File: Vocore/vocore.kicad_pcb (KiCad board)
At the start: 4 copper layers, 58 x 58 mm, 126 parts, among them IC1 IC_ATMEGA32U4_TQFP44, J1 IO_USB-MICRO-B-MK5P, P2 IO_HOLE-3.2, P3 IO_HOLE-3.2, P3 PINHOLE, U1 IC_MP1484EN_SOIC08, U10 DLW21SN900SQ2, U11 C_SW_SPSDSMD, U13 IP4220CZ6, U14 IP4220CZ6, U15 AP2146, U16 AP2146, U17 C_SW_SPSDSMD, U2 DLW21SN900SQ2, U3 IP4220CZ6, U4 UPD720114-QFP48, U5 USB-AF-90, U8 FT232RL_SSOP_28, U9 DLW21SN900SQ2, X1 30MHz, X2 16m

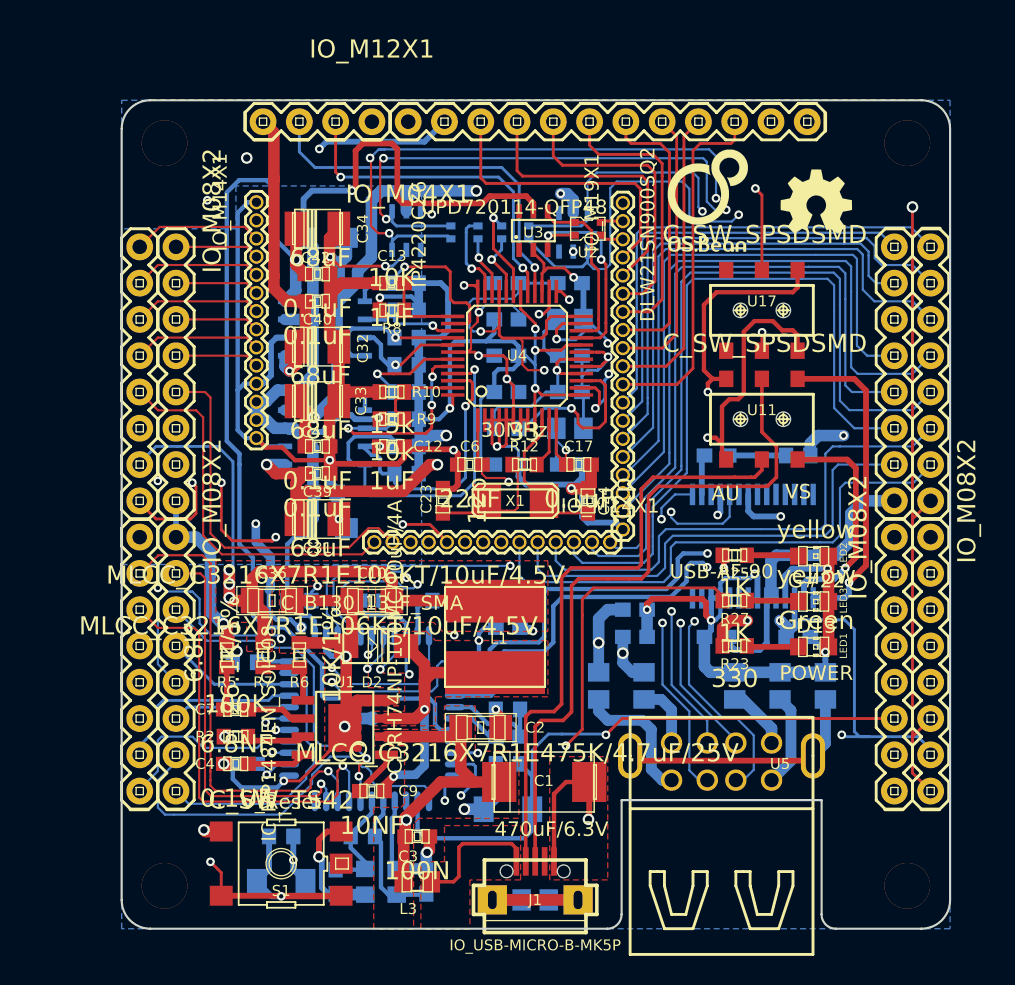
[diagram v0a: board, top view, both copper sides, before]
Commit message: Vocore第二版修改完成
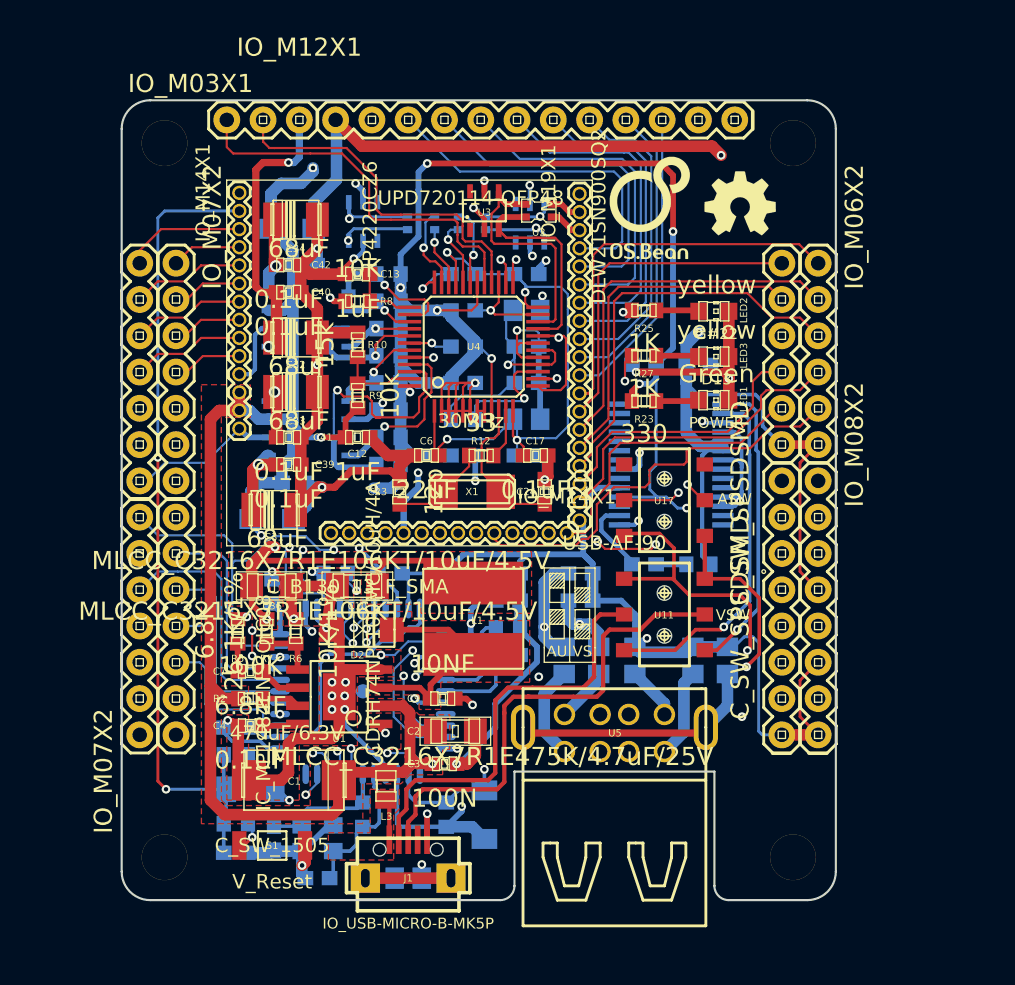
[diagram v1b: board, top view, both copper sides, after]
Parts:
- added C48: 104, C_C_0603, B.Cu at (87.0, 130.7)
- added R28: 200, C_R_0603, B.Cu at (87.0, 128.7)
- JP4: value IO_M08X2 -> IO_M06X2; footprint IO_M08X2 -> IO_M06X2
- JP5, JP6: value IO_M08X2 -> IO_M07X2; footprint IO_M08X2 -> IO_M07X2
- JP9: value IO_M04X1 -> IO_M03X1; footprint IO_M04X1 -> IO_M03X1
- S1: value C_SW_TS42 -> C_SW_1505; footprint C_SW_TS42 -> C_SW_1505
- moved JP6 55.3 mm to (82.8, 122.4)
- moved JP4 48.9 mm to (125.2, 89.4)
- moved C46 21.9 mm to (115.6, 96.5), turned to 0 degrees
- moved C47 19.1 mm to (119.4, 96.5), turned to 180 degrees
- moved LED1 18.6 mm to (120.7, 98.9)
- moved LED2 18.5 mm to (120.7, 92.7)
- moved LED3 18.5 mm to (120.7, 95.9)
- moved R25 18.3 mm to (115.6, 92.7)
- moved R23 18.3 mm to (115.6, 99.1)
- moved R27 18.3 mm to (115.6, 95.9)
- moved C1 17.5 mm to (91.1, 125.6), turned to 180 degrees
- moved U11 15.3 mm to (117.0, 114.0), turned to 90 degrees
- moved U17 14.9 mm to (117.0, 106.0), turned to 90 degrees
- moved R26 10.3 mm to (119.4, 110.5)
- moved JP9 10.2 mm to (86.4, 79.4), turned to 180 degrees
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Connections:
- JP2 pad 2: /G#26/LED4 -> (no net)
- JP2 pad 3: /G#25/LED3 -> (no net)
- JP2 pad 4: /G#24/LED2 -> (no net)
- JP2 pad 6: /G#23/LED1 -> (no net)
- JP3 pad 1: +3.3V -> (no net)
- JP4 pad 1: +5V -> /G#03/SPI_CS0
- JP4 pad 10: /ATMEGA32U4/D7 -> /G#13/PCM_DRX
- JP4 pad 11: /ATMEGA32U4/IO8 -> +5V
- JP4 pad 12: /ATMEGA32U4/IO9* -> +5V
- JP4 pad 2: GND -> /G#11/PCM_FS
- JP4 pad 3: /ATMEGA32U4/D0/RX -> /G#10/I2S_SDI/RXD
- JP4 pad 4: /ATMEGA32U4/D1/TX -> /G#06/SPI_MISO
- JP4 pad 5: /ATMEGA32U4/D2/SDA -> /G#08/I2S_WS/TDX
- JP4 pad 6: /ATMEGA32U4/D3/SCL -> /G#16/RXD2
- JP4 pad 7: /ATMEGA32U4/D4 -> /G#07/I2S_CLK
- JP4 pad 8: /ATMEGA32U4/D5* -> /G#15/TXD2
- JP4 pad 9: /ATMEGA32U4/D6* -> /G#14/PCM_DTX
- JP5 pad 10: /G#09/I2S_SD0 -> /G#05/SPI_MOSI
- JP5 pad 11: /G#05/SPI_MOSI -> /G#04/SPI_CLK
- JP5 pad 12: /G#04/SPI_CLK -> /G#09/I2S_SD0
- JP5 pad 13: +3.3V -> GND
- JP5 pad 14: /G#27/SPI_CS1 -> /G#12/PCM_CLK
- JP5 pad 9: /G#12/PCM_CLK -> /G#27/SPI_CS1
- JP6 pad 1: GND -> /ATMEGA32U4/D0/RX
- JP6 pad 10: /G#07/I2S_CLK -> /ATMEGA32U4/IO9*
- JP6 pad 11: /G#16/RXD2 -> /ATMEGA32U4/IO10*
- JP6 pad 12: /G#08/I2S_WS/TDX -> /ATMEGA32U4/IO11*
- JP6 pad 13: /G#06/SPI_MISO -> /ATMEGA32U4/IO12
- JP6 pad 14: /G#10/I2S_SDI/RXD -> /ATMEGA32U4/IO13*
- JP6 pad 2: +5V -> /ATMEGA32U4/D1/TX
- JP6 pad 3: /G#23/LED1 -> /ATMEGA32U4/D2/SDA
- JP6 pad 4: /G#13/PCM_DRX -> /ATMEGA32U4/D3/SCL
- JP6 pad 5: /G#24/LED2 -> /ATMEGA32U4/D4
- JP6 pad 6: /G#25/LED3 -> /ATMEGA32U4/D5*
- JP6 pad 7: /G#26/LED4 -> /ATMEGA32U4/D6*
- JP6 pad 8: /G#14/PCM_DTX -> /ATMEGA32U4/D7
- JP6 pad 9: /G#15/TXD2 -> /ATMEGA32U4/IO8
- JP7 pad 15: +5V -> GND
- JP9 pad 1: GND -> /uPD720114/DP2
- JP9 pad 2: /uPD720114/DP2 -> /uPD720114/DM2
- JP9 pad 3: /uPD720114/DM2 -> /uPD720114/VBUS3
- S1 pad 1: /RESET -> GND
- S1 pad 2: /RESET -> N-0000048
- U8 pad 1: /G#15/TXD2 -> /G#16/RXD2
- U8 pad 5: /G#16/RXD2 -> /G#15/TXD2
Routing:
- net GND: track 484.4 -> 362.3 mm, vias 42 -> 36
- net /G#26/LED4: track 51.6 -> 0.00 mm
- net /G#25/LED3: track 50.8 -> 0.00 mm
- net +3.3V: track 293.8 -> 245.1 mm, vias 14 -> 16
- net /uPD720114/VBUS2: track 112.7 -> 70.4 mm
- net /+1.8V: track 100.6 -> 58.4 mm, vias 6 -> 1
- net /uPD720114/VBUS1: track 120.4 -> 78.2 mm, vias 4 -> 3
- net /G#23/LED1: track 37.8 -> 0.00 mm
- net /G#24/LED2: track 35.9 -> 0.00 mm
- net +5V: track 274.1 -> 243.1 mm, vias 8 -> 10
- net /G#08/I2S_WS/TDX: track 72.6 -> 42.5 mm, vias 0 -> 2
- net /G#15/TXD2: track 51.0 -> 25.4 mm, vias 1 -> 0
- net /G#14/PCM_DTX: track 46.1 -> 20.9 mm
- net /G#07/I2S_CLK: track 40.2 -> 19.3 mm
- net /ATMEGA32U4/A4: track 54.1 -> 33.4 mm
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- added copper zone on Inner1.Cu, net GND
- removed copper zone on B.Cu, net GND
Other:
- board size 58 x 58 mm -> 50 x 56 mm
- board text added: "ASW"
- board text added: "G#01"
- board text added: "G#02"
- board text added: "G#03"
- board text added: "G#04"
- board text added: "G#05"
- board text added: "G#06"
- board text added: "G#07"
- board text added: "G#08"
- board text added: "G#09"
- board text added: "G#10"
- board text added: "G#11"
- board text added: "G#12"
- board text added: "G#13"
- board text added: "G#14"
- board text added: "G#15"
- board text added: "G#16"
- board text added: "G#17"
- board text added: "G#18"
- board text added: "G#19"
- board text added: "G#20"
- board text added: "G#21"
- board text added: "G#27"
- board text added: "VSW"
- board text removed: "3.3V"
- board text removed: "CS0"
- board text removed: "CS1"
- board text removed: "DRX"
- board text removed: "DTX"
- board text removed: "FS"
- board text removed: "I_CLK"
- board text removed: "LED1"
- board text removed: "LED2"
- board text removed: "LED3"
- board text removed: "LED4"
- board text removed: "P_CLK"
- board text removed: "RXD"
- board text removed: "RXD2"
- board text removed: "SCLK"
- board text removed: "SD"
- board text removed: "SD0"
- board text removed: "S_CLK"
- board text removed: "S_SI"
- board text removed: "S_SO"
- board text removed: "TCLK"
- board text removed: "TD0"
- board text removed: "TDI"
- board text removed: "TDX"
- board text removed: "TMS"
- board text removed: "TRST"
- board text removed: "TXD2"

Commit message: modify  PCB
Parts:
- removed JP3: IO_M19X1, IO-M19X1-1.27MM
- added JP10: IO_M18X1, IO-M18X1-1.27MM, F.Cu at (111.1, 84.6)
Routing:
- net GND: track 362.3 -> 360.4 mm
- net (no net): track 0.00 -> 1.88 mm
- net /P0TN: vias 1 -> 0
- added copper zone on F.Cu, net N-0000042
- removed copper zone on F.Cu, net N-0000036
